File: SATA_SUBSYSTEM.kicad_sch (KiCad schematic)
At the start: 0 parts

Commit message: Transferred everything to hierarchical schematic and wired PSU power on circuit AND created duplicate schematics for all relevant subsystems
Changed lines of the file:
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@@
 	)
 	(hierarchical_label "5V_FLT_CTRL"
-		(shape input)
+		(shape output)
 		(at 87.63 58.42 180)
 		(effects
@@
 	)
 	(hierarchical_label "12V_FLT_CTRL"
-		(shape input)
+		(shape output)
 		(at 87.63 78.74 180)
 		(effects
@@
 		(dnp no)
 		(fields_autoplaced yes)
-		(property "Reference" "#PWR013"
+		(property "Reference" "#PWR0121"
 			(at 50.8 88.9 0)
 			(hide yes)
@@
 		(instances
 			(project "serverv2_backplane"
+				(path "/d38d6818-cf53-410d-afa3-a75a85b7c05a/1271a149-7432-404a-bbd5-7ae0b7a8d68d"
+					(reference "#PWR0817")
+					(unit 1)
+				)
+				(path "/d38d6818-cf53-410d-afa3-a75a85b7c05a/2b34bdfe-333e-4210-8353-2d6d8e14690a"
+					(reference "#PWR0700")
+					(unit 1)
+				)
+				(path "/d38d6818-cf53-410d-afa3-a75a85b7c05a/2b409005-8f0c-424d-bea3-7f99170f3949"
+					(reference "#PWR0334")
+					(unit 1)
+				)
+				(path "/d38d6818-cf53-410d-afa3-a75a85b7c05a/46262d05-a782-4c24-8fee-232f080edae1"
+					(reference "#PWR0641")
+					(unit 1)
+				)
+				(path "/d38d6818-cf53-410d-afa3-a75a85b7c05a/470b220a-a565-4e43-ab90-9eb03ea2cd43"
+					(reference "#PWR0520")
+					(unit 1)
+				)
 				(path "/d38d6818-cf53-410d-afa3-a75a85b7c05a/4cfb14a9-2f19-498b-8efa-0b74e4ca5f47"
 					(reference "#PWR013")
+					(unit 1)
+				)
+				(path "/d38d6818-cf53-410d-afa3-a75a85b7c05a/50af50d7-94b3-4b11-b0b0-fb1dfb06c699"
+					(reference "#PWR0818")
+					(unit 1)
+				)
+				(path "/d38d6818-cf53-410d-afa3-a75a85b7c05a/8533a259-5737-4fce-b4c0-279539c49b16"
+					(reference "#PWR0819")
+					(unit 1)
+				)
+				(path "/d38d6818-cf53-410d-afa3-a75a85b7c05a/a91f2db0-df6c-4013-b7b0-c2c51c5a6ec1"
+					(reference "#PWR0105")
+					(unit 1)
+				)
+				(path "/d38d6818-cf53-410d-afa3-a75a85b7c05a/bfbdef84-70db-44df-9f2c-b3e154a7a6cb"
+					(reference "#PWR0121")
+					(unit 1)
+				)
+				(path "/d38d6818-cf53-410d-afa3-a75a85b7c05a/c1d5cf6d-a75d-4df1-9c1d-6d5e2a990df7"
+					(reference "#PWR0748")
+					(unit 1)
+				)
+				(path "/d38d6818-cf53-410d-afa3-a75a85b7c05a/ca25108c-b61e-40df-845b-d107b2a6dbc6"
+					(reference "#PWR0953")
 					(unit 1)
 				)
@@
 			)
 		)
-		(pin "5V_FLT_CTRL" input
+		(pin "5V_FLT_CTRL" output
 			(at 90.17 58.42 180)
 			(effects
@@
 				(path "/d38d6818-cf53-410d-afa3-a75a85b7c05a/4cfb14a9-2f19-498b-8efa-0b74e4ca5f47"
 					(page "19")
+				)
+				(path "/d38d6818-cf53-410d-afa3-a75a85b7c05a/bfbdef84-70db-44df-9f2c-b3e154a7a6cb"
+					(page "43")
+				)
+				(path "/d38d6818-cf53-410d-afa3-a75a85b7c05a/470b220a-a565-4e43-ab90-9eb03ea2cd43"
+					(page "49")
+				)
+				(path "/d38d6818-cf53-410d-afa3-a75a85b7c05a/a91f2db0-df6c-4013-b7b0-c2c51c5a6ec1"
+					(page "55")
+				)
+				(path "/d38d6818-cf53-410d-afa3-a75a85b7c05a/2b409005-8f0c-424d-bea3-7f99170f3949"
+					(page "61")
+				)
+				(path "/d38d6818-cf53-410d-afa3-a75a85b7c05a/46262d05-a782-4c24-8fee-232f080edae1"
+					(page "67")
+				)
+				(path "/d38d6818-cf53-410d-afa3-a75a85b7c05a/2b34bdfe-333e-4210-8353-2d6d8e14690a"
+					(page "74")
+				)
+				(path "/d38d6818-cf53-410d-afa3-a75a85b7c05a/c1d5cf6d-a75d-4df1-9c1d-6d5e2a990df7"
+					(page "80")
+				)
+				(path "/d38d6818-cf53-410d-afa3-a75a85b7c05a/50af50d7-94b3-4b11-b0b0-fb1dfb06c699"
+					(page "87")
+				)
+				(path "/d38d6818-cf53-410d-afa3-a75a85b7c05a/1271a149-7432-404a-bbd5-7ae0b7a8d68d"
+					(page "93")
+				)
+				(path "/d38d6818-cf53-410d-afa3-a75a85b7c05a/8533a259-5737-4fce-b4c0-279539c49b16"
+					(page "99")
+				)
+				(path "/d38d6818-cf53-410d-afa3-a75a85b7c05a/ca25108c-b61e-40df-845b-d107b2a6dbc6"
+					(page "105")
 				)
 			)
@@
 					(page "16")
 				)
+				(path "/d38d6818-cf53-410d-afa3-a75a85b7c05a/bfbdef84-70db-44df-9f2c-b3e154a7a6cb"
+					(page "42")
+				)
+				(path "/d38d6818-cf53-410d-afa3-a75a85b7c05a/470b220a-a565-4e43-ab90-9eb03ea2cd43"
+					(page "48")
+				)
+				(path "/d38d6818-cf53-410d-afa3-a75a85b7c05a/a91f2db0-df6c-4013-b7b0-c2c51c5a6ec1"
+					(page "54")
+				)
+				(path "/d38d6818-cf53-410d-afa3-a75a85b7c05a/2b409005-8f0c-424d-bea3-7f99170f3949"
+					(page "60")
+				)
+				(path "/d38d6818-cf53-410d-afa3-a75a85b7c05a/46262d05-a782-4c24-8fee-232f080edae1"
+					(page "66")
+				)
+				(path "/d38d6818-cf53-410d-afa3-a75a85b7c05a/2b34bdfe-333e-4210-8353-2d6d8e14690a"
+					(page "73")
+				)
+				(path "/d38d6818-cf53-410d-afa3-a75a85b7c05a/c1d5cf6d-a75d-4df1-9c1d-6d5e2a990df7"
+					(page "79")
+				)
+				(path "/d38d6818-cf53-410d-afa3-a75a85b7c05a/50af50d7-94b3-4b11-b0b0-fb1dfb06c699"
+					(page "86")
+				)
+				(path "/d38d6818-cf53-410d-afa3-a75a85b7c05a/1271a149-7432-404a-bbd5-7ae0b7a8d68d"
+					(page "92")
+				)
+				(path "/d38d6818-cf53-410d-afa3-a75a85b7c05a/8533a259-5737-4fce-b4c0-279539c49b16"
+					(page "98")
+				)
+				(path "/d38d6818-cf53-410d-afa3-a75a85b7c05a/ca25108c-b61e-40df-845b-d107b2a6dbc6"
+					(page "104")
+				)
 			)
 		)
@@
 			)
 		)
-		(pin "12V_FLT_CTRL" input
+		(pin "12V_FLT_CTRL" output
 			(at 90.17 78.74 180)
 			(effects
@@
 				(path "/d38d6818-cf53-410d-afa3-a75a85b7c05a/4cfb14a9-2f19-498b-8efa-0b74e4ca5f47"
 					(page "20")
+				)
+				(path "/d38d6818-cf53-410d-afa3-a75a85b7c05a/bfbdef84-70db-44df-9f2c-b3e154a7a6cb"
+					(page "41")
+				)
+				(path "/d38d6818-cf53-410d-afa3-a75a85b7c05a/470b220a-a565-4e43-ab90-9eb03ea2cd43"
+					(page "47")
+				)
+				(path "/d38d6818-cf53-410d-afa3-a75a85b7c05a/a91f2db0-df6c-4013-b7b0-c2c51c5a6ec1"
+					(page "53")
+				)
+				(path "/d38d6818-cf53-410d-afa3-a75a85b7c05a/2b409005-8f0c-424d-bea3-7f99170f3949"
+					(page "59")
+				)
+				(path "/d38d6818-cf53-410d-afa3-a75a85b7c05a/46262d05-a782-4c24-8fee-232f080edae1"
+					(page "65")
+				)
+				(path "/d38d6818-cf53-410d-afa3-a75a85b7c05a/2b34bdfe-333e-4210-8353-2d6d8e14690a"
+					(page "72")
+				)
+				(path "/d38d6818-cf53-410d-afa3-a75a85b7c05a/c1d5cf6d-a75d-4df1-9c1d-6d5e2a990df7"
+					(page "78")
+				)
+				(path "/d38d6818-cf53-410d-afa3-a75a85b7c05a/50af50d7-94b3-4b11-b0b0-fb1dfb06c699"
+					(page "85")
+				)
+				(path "/d38d6818-cf53-410d-afa3-a75a85b7c05a/1271a149-7432-404a-bbd5-7ae0b7a8d68d"
+					(page "91")
+				)
+				(path "/d38d6818-cf53-410d-afa3-a75a85b7c05a/8533a259-5737-4fce-b4c0-279539c49b16"
+					(page "97")
+				)
+				(path "/d38d6818-cf53-410d-afa3-a75a85b7c05a/ca25108c-b61e-40df-845b-d107b2a6dbc6"
+					(page "103")
 				)
 			)
@@
 					(page "18")
 				)
+				(path "/d38d6818-cf53-410d-afa3-a75a85b7c05a/bfbdef84-70db-44df-9f2c-b3e154a7a6cb"
+					(page "44")
+				)
+				(path "/d38d6818-cf53-410d-afa3-a75a85b7c05a/470b220a-a565-4e43-ab90-9eb03ea2cd43"
+					(page "50")
+				)
+				(path "/d38d6818-cf53-410d-afa3-a75a85b7c05a/a91f2db0-df6c-4013-b7b0-c2c51c5a6ec1"
+					(page "56")
+				)
+				(path "/d38d6818-cf53-410d-afa3-a75a85b7c05a/2b409005-8f0c-424d-bea3-7f99170f3949"
+					(page "62")
+				)
+				(path "/d38d6818-cf53-410d-afa3-a75a85b7c05a/46262d05-a782-4c24-8fee-232f080edae1"
+					(page "68")
+				)
+				(path "/d38d6818-cf53-410d-afa3-a75a85b7c05a/2b34bdfe-333e-4210-8353-2d6d8e14690a"
+					(page "75")
+				)
+				(path "/d38d6818-cf53-410d-afa3-a75a85b7c05a/c1d5cf6d-a75d-4df1-9c1d-6d5e2a990df7"
+					(page "81")
+				)
+				(path "/d38d6818-cf53-410d-afa3-a75a85b7c05a/50af50d7-94b3-4b11-b0b0-fb1dfb06c699"
+					(page "88")
+				)
+				(path "/d38d6818-cf53-410d-afa3-a75a85b7c05a/1271a149-7432-404a-bbd5-7ae0b7a8d68d"
+					(page "94")
+				)
+				(path "/d38d6818-cf53-410d-afa3-a75a85b7c05a/8533a259-5737-4fce-b4c0-279539c49b16"
+					(page "100")
+				)
+				(path "/d38d6818-cf53-410d-afa3-a75a85b7c05a/ca25108c-b61e-40df-845b-d107b2a6dbc6"
+					(page "106")
+				)
 			)
 		)
@@
 					(page "17")
 				)
-			)
+				(path "/d38d6818-cf53-410d-afa3-a75a85b7c05a/bfbdef84-70db-44df-9f2c-b3e154a7a6cb"
+					(page "45")
+				)
+				(path "/d38d6818-cf53-410d-afa3-a75a85b7c05a/470b220a-a565-4e43-ab90-9eb03ea2cd43"
+					(page "51")
+				)
+				(path "/d38d6818-cf53-410d-afa3-a75a85b7c05a/a91f2db0-df6c-4013-b7b0-c2c51c5a6ec1"
+					(page "57")
+				)
+				(path "/d38d6818-cf53-410d-afa3-a75a85b7c05a/2b409005-8f0c-424d-bea3-7f99170f3949"
+					(page "63")
+				)
+				(path "/d38d6818-cf53-410d-afa3-a75a85b7c05a/46262d05-a782-4c24-8fee-232f080edae1"
+					(page "69")
+				)
+				(path "/d38d6818-cf53-410d-afa3-a75a85b7c05a/2b34bdfe-333e-4210-8353-2d6d8e14690a"
+					(page "76")
+				)
+				(path "/d38d6818-cf53-410d-afa3-a75a85b7c05a/c1d5cf6d-a75d-4df1-9c1d-6d5e2a990df7"
+					(page "82")
+				)
+				(path "/d38d6818-cf53-410d-afa3-a75a85b7c05a/50af50d7-94b3-4b11-b0b0-fb1dfb06c699"
+					(page "89")
+				)
+				(path "/d38d6818-cf53-410d-afa3-a75a85b7c05a/1271a149-7432-404a-bbd5-7ae0b7a8d68d"
+					(page "95")
+				)
+				(path "/d38d6818-cf53-410d-afa3-a75a85b7c05a/8533a259-5737-4fce-b4c0-279539c49b16"
+					(page "101")
+				)
+				(path "/d38d6818-cf53-410d-afa3-a75a85b7c05a/ca25108c-b61e-40df-845b-d107b2a6dbc6"
+					(page "107")
+				)
+			)

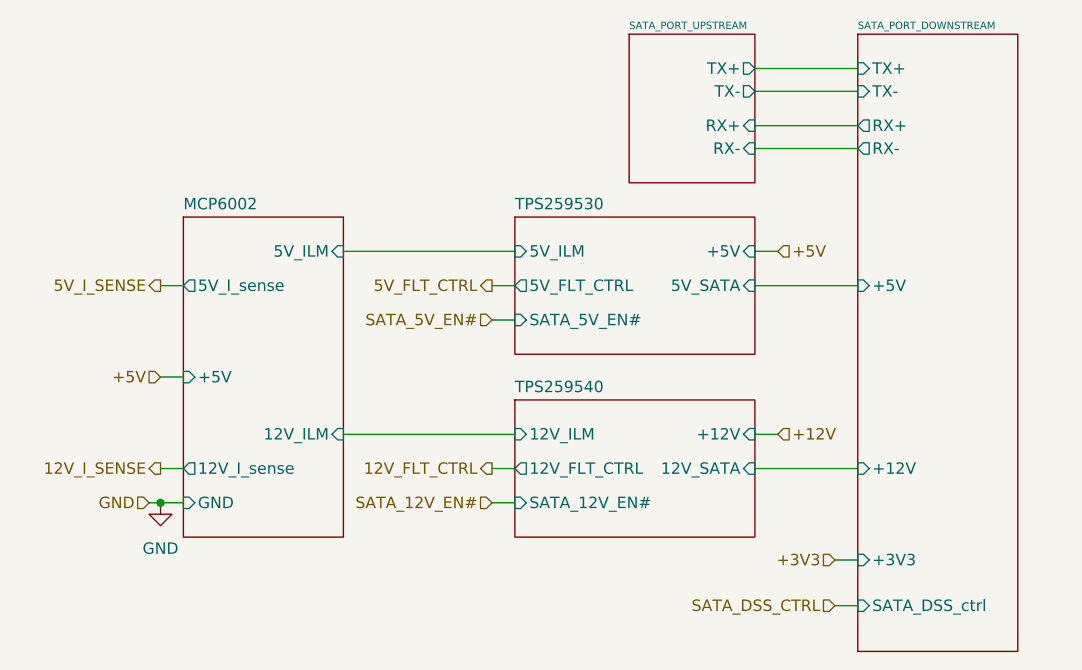
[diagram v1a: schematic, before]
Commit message: Cleaned up schematic and replaced TC358743XBG with reverse-engineered LT6911C
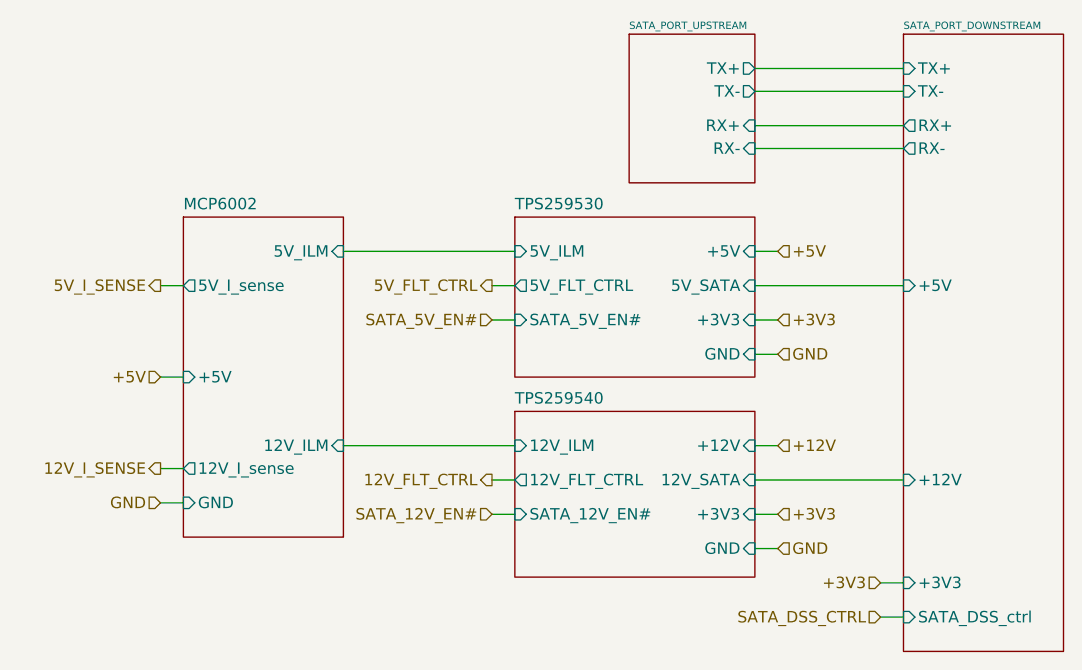
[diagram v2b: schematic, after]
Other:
- sheet TPS259530 ports: added +3V3, GND; removed none
- sheet TPS259540 ports: added +3V3, GND; removed none

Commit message: Added TVS clamping diodes to upstream USB-C port and fixed RX/TX orientation routing for entire system
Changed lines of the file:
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@@
+	(wire
+		(pts
+			(xy 116.84 34.29) (xy 133.35 34.29)
+		)
+		(stroke
+			(width 0)
+			(type default)
+		)
+	)
+	(wire
+		(pts
+			(xy 116.84 40.64) (xy 133.35 40.64)
+		)
+		(stroke
+			(width 0)
+			(type default)
+		)
+	)
 	(wire
 		(pts
@@
 	(wire
 		(pts
+			(xy 130.81 91.44) (xy 133.35 91.44)
+		)
+		(stroke
+			(width 0)
+			(type default)
+		)
+	)
+	(wire
+		(pts
+			(xy 119.38 76.2) (xy 116.84 76.2)
+		)
+		(stroke
+			(width 0)
+			(type default)
+		)
+	)
+	(wire
+		(pts
+			(xy 50.8 82.55) (xy 53.34 82.55)
+		)
+		(stroke
+			(width 0)
+			(type default)
+		)
+	)
+	(wire
+		(pts
+			(xy 50.8 78.74) (xy 53.34 78.74)
+		)
+		(stroke
+			(width 0)
+			(type default)
+		)
+	)
+	(wire
+		(pts
+			(xy 87.63 80.01) (xy 90.17 80.01)
+		)
+		(stroke
+			(width 0)
+			(type default)
+		)
+	)
+	(wire
+		(pts
+			(xy 71.12 54.61) (xy 90.17 54.61)
+		)
+		(stroke
+			(width 0)
+			(type default)
+		)
+	)
+	(wire
+		(pts
 			(xy 116.84 36.83) (xy 133.35 36.83)
 		)
@@
 	(wire
 		(pts
-			(xy 130.81 91.44) (xy 133.35 91.44)
-		)
-		(stroke
-			(width 0)
-			(type default)
-		)
-	)
-	(wire
-		(pts
-			(xy 119.38 76.2) (xy 116.84 76.2)
-		)
-		(stroke
-			(width 0)
-			(type default)
-		)
-	)
-	(wire
-		(pts
-			(xy 50.8 82.55) (xy 53.34 82.55)
-		)
-		(stroke
-			(width 0)
-			(type default)
-		)
-	)
-	(wire
-		(pts
-			(xy 50.8 78.74) (xy 53.34 78.74)
-		)
-		(stroke
-			(width 0)
-			(type default)
-		)
-	)
-	(wire
-		(pts
-			(xy 87.63 80.01) (xy 90.17 80.01)
-		)
-		(stroke
-			(width 0)
-			(type default)
-		)
-	)
-	(wire
-		(pts
-			(xy 71.12 54.61) (xy 90.17 54.61)
-		)
-		(stroke
-			(width 0)
-			(type default)
-		)
-	)
-	(wire
-		(pts
-			(xy 116.84 34.29) (xy 133.35 34.29)
-		)
-		(stroke
-			(width 0)
-			(type default)
-		)
-	)
-	(wire
-		(pts
-			(xy 116.84 40.64) (xy 133.35 40.64)
+			(xy 116.84 83.82) (xy 119.38 83.82)
+		)
+		(stroke
+			(width 0)
+			(type default)
+		)
+	)
+	(wire
+		(pts
+			(xy 87.63 62.23) (xy 90.17 62.23)
+		)
+		(stroke
+			(width 0)
+			(type default)
+		)
+	)
+	(wire
+		(pts
+			(xy 116.84 80.01) (xy 133.35 80.01)
+		)
+		(stroke
+			(width 0)
+			(type default)
+		)
+	)
+	(wire
+		(pts
+			(xy 119.38 62.23) (xy 116.84 62.23)
+		)
+		(stroke
+			(width 0)
+			(type default)
+		)
+	)
+	(wire
+		(pts
+			(xy 71.12 76.2) (xy 90.17 76.2)
+		)
+		(stroke
+			(width 0)
+			(type default)
+		)
+	)
+	(wire
+		(pts
+			(xy 116.84 58.42) (xy 133.35 58.42)
+		)
+		(stroke
+			(width 0)
+			(type default)
+		)
+	)
+	(wire
+		(pts
+			(xy 87.63 83.82) (xy 90.17 83.82)
+		)
+		(stroke
+			(width 0)
+			(type default)
+		)
+	)
+	(wire
+		(pts
+			(xy 119.38 66.04) (xy 116.84 66.04)
 		)
 		(stroke
@@
 		(pts
 			(xy 116.84 43.18) (xy 133.35 43.18)
-		)
-		(stroke
-			(width 0)
-			(type default)
-		)
-	)
-	(wire
-		(pts
-			(xy 116.84 83.82) (xy 119.38 83.82)
-		)
-		(stroke
-			(width 0)
-			(type default)
-		)
-	)
-	(wire
-		(pts
-			(xy 87.63 62.23) (xy 90.17 62.23)
-		)
-		(stroke
-			(width 0)
-			(type default)
-		)
-	)
-	(wire
-		(pts
-			(xy 116.84 80.01) (xy 133.35 80.01)
-		)
-		(stroke
-			(width 0)
-			(type default)
-		)
-	)
-	(wire
-		(pts
-			(xy 119.38 62.23) (xy 116.84 62.23)
-		)
-		(stroke
-			(width 0)
-			(type default)
-		)
-	)
-	(wire
-		(pts
-			(xy 71.12 76.2) (xy 90.17 76.2)
-		)
-		(stroke
-			(width 0)
-			(type default)
-		)
-	)
-	(wire
-		(pts
-			(xy 116.84 58.42) (xy 133.35 58.42)
-		)
-		(stroke
-			(width 0)
-			(type default)
-		)
-	)
-	(wire
-		(pts
-			(xy 87.63 83.82) (xy 90.17 83.82)
-		)
-		(stroke
-			(width 0)
-			(type default)
-		)
-	)
-	(wire
-		(pts
-			(xy 119.38 66.04) (xy 116.84 66.04)
 		)
 		(stroke
@@
 		)
 		(pin "TX+" output
+			(at 116.84 40.64 0)
+			(effects
+				(font
+					(size 1.27 1.27)
+				)
+				(justify right)
+			)
+		)
+		(pin "RX-" input
+			(at 116.84 36.83 0)
+			(effects
+				(font
+					(size 1.27 1.27)
+				)
+				(justify right)
+			)
+		)
+		(pin "TX-" output
+			(at 116.84 43.18 0)
+			(effects
+				(font
+					(size 1.27 1.27)
+				)
+				(justify right)
+			)
+		)
+		(pin "RX+" input
 			(at 116.84 34.29 0)
-			(effects
-				(font
-					(size 1.27 1.27)
-				)
-				(justify right)
-			)
-		)
-		(pin "RX-" input
-			(at 116.84 43.18 0)
-			(effects
-				(font
-					(size 1.27 1.27)
-				)
-				(justify right)
-			)
-		)
-		(pin "TX-" output
-			(at 116.84 36.83 0)
-			(effects
-				(font
-					(size 1.27 1.27)
-				)
-				(justify right)
-			)
-		)
-		(pin "RX+" input
-			(at 116.84 40.64 0)
 			(effects
 				(font
@@
 			)
 		)
-		(pin "TX-" input
+		(pin "TX-" output
 			(at 133.35 36.83 180)
 			(effects
@@
 			)
 		)
-		(pin "RX+" output
+		(pin "RX+" input
 			(at 133.35 40.64 180)
 			(effects
@@
 			)
 		)
-		(pin "TX+" input
+		(pin "TX+" output
 			(at 133.35 34.29 180)
 			(effects
@@
 			)
 		)
-		(pin "RX-" output
+		(pin "RX-" input
 			(at 133.35 43.18 180)
 			(effects
